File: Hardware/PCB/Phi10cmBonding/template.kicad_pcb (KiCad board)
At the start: 4 copper layers, 38.1 x 38.1 mm, 0 parts

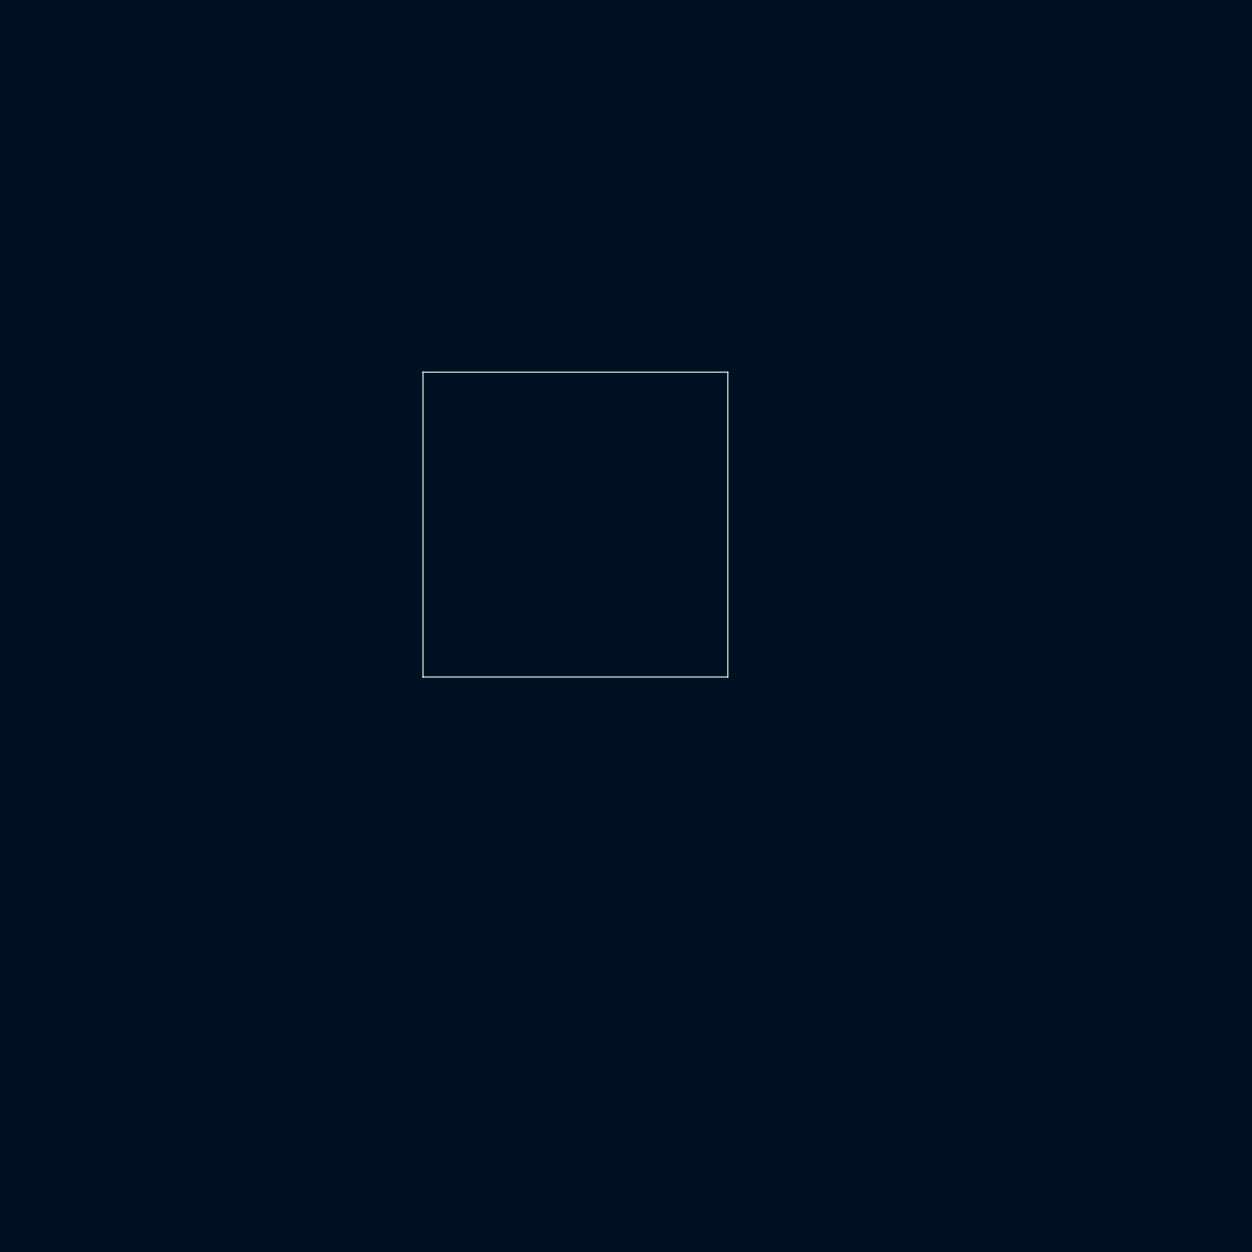
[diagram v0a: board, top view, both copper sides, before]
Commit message: Achieve reasonable array generation.
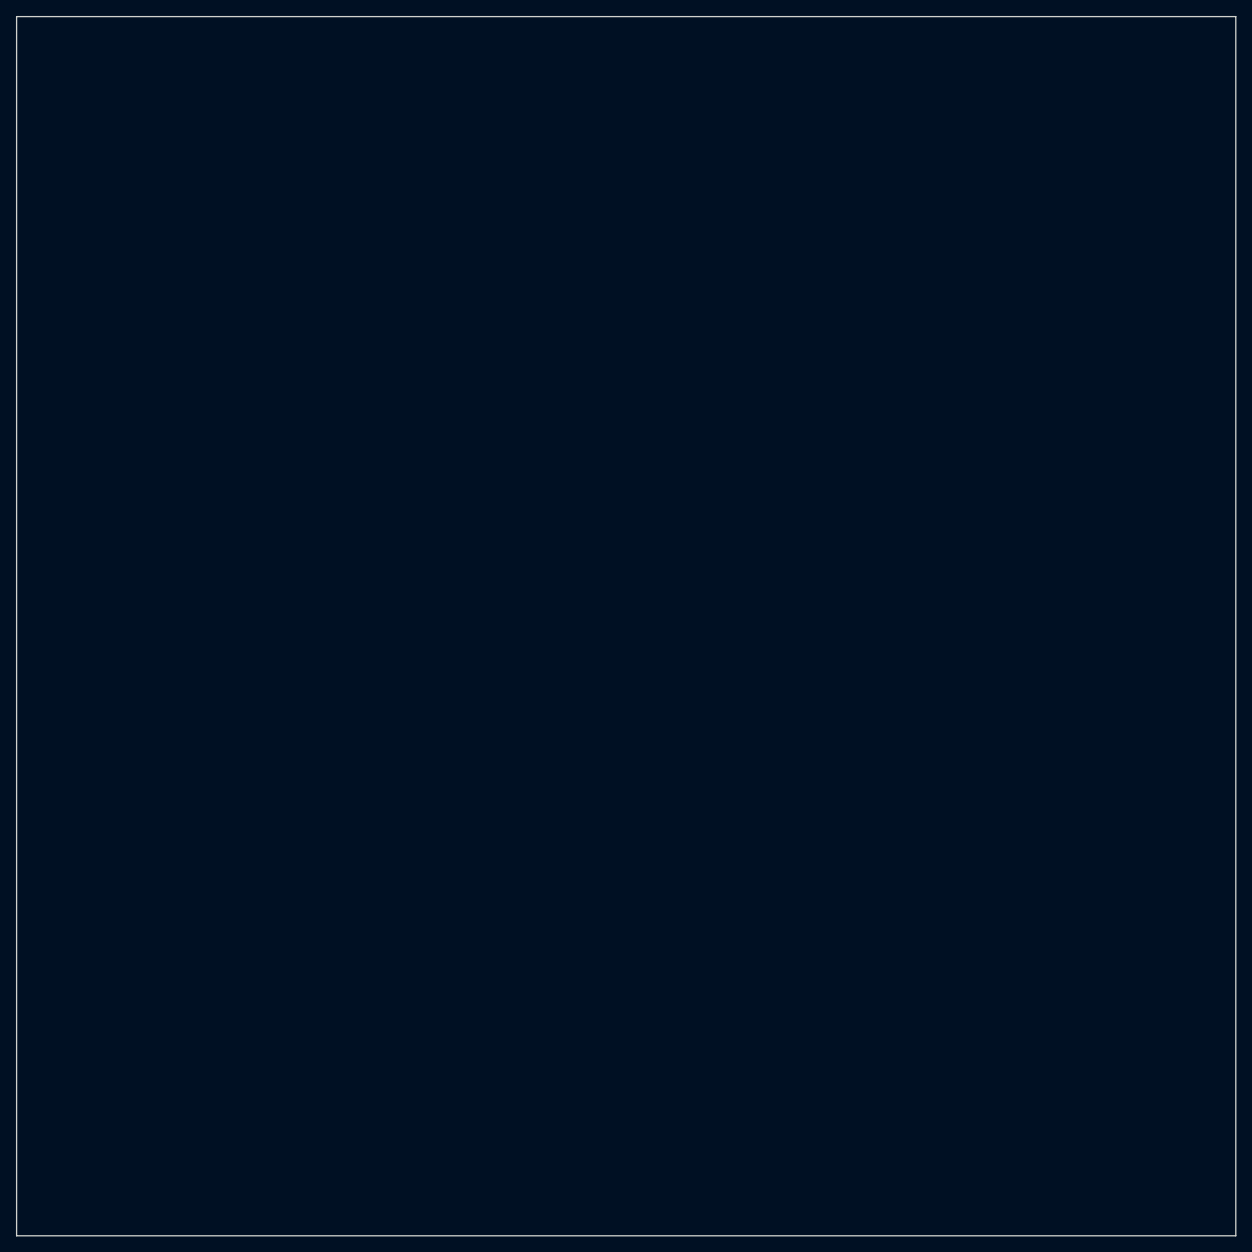
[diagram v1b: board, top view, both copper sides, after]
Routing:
- removed copper zone on In1.Cu, net /GND
- removed copper zone on In2.Cu, net /VDD
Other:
- board size 38.1 x 38.1 mm -> 152.4 x 152.4 mm
- copper layers 4 -> 20
- net class Default: trace_width 0.1524 -> 0.1016; via_dia 0.508 -> 0.5588; via_drill 0.381 -> 0.2032
- rule trace_min: 0.1524 -> 0.1016
- rule via_min_drill: 0.381 -> 0.2032
- rule via_min_size: 0.508 -> 0.5588
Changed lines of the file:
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@@
     (links 0)
     (no_connects 0)
-    (area 114.224999 76.124999 152.475001 114.375001)
-    (thickness 1.6)
+    (area 63.424999 31.674999 215.975001 184.225001)
+    (thickness 3.175)
     (drawings 4)
     (tracks 0)
     (zones 0)
     (modules 0)
-    (nets 3)
+    (nets 1)
   )
   (page USLetter)
@@
     (0 F.Cu signal)
     (1 In1.Cu power)
-    (2 In2.Cu jumper)
+    (2 In2.Cu signal)
+    (3 In3.Cu signal)
+    (4 In4.Cu signal)
+    (5 In5.Cu signal)
+    (6 In6.Cu signal)
+    (7 In7.Cu signal)
+    (8 In8.Cu signal)
+    (9 In9.Cu signal)
+    (10 In10.Cu signal)
+    (11 In11.Cu signal)
+    (12 In12.Cu signal)
+    (13 In13.Cu signal)
+    (14 In14.Cu signal)
+    (15 In15.Cu signal)
+    (16 In16.Cu signal)
+    (17 In17.Cu signal)
+    (18 In18.Cu signal)
     (31 B.Cu signal)
     (33 F.Adhes user)
@@
   )
   (setup
-    (last_trace_width 0.1524)
+    (last_trace_width 0.1016)
+    (user_trace_width 0.1016)
     (user_trace_width 0.1524)
     (user_trace_width 0.2032)
@@
     (zone_clearance 0.508)
     (zone_45_only no)
-    (trace_min 0.1524)
+    (trace_min 0.1016)
     (segment_width 0.2)
     (edge_width 0.15)
-    (via_size 0.508)
-    (via_drill 0.381)
-    (via_min_size 0.508)
-    (via_min_drill 0.381)
-    (user_via 0.508 0.381)
-    (user_via 0.762 0.508)
+    (via_size 0.5588)
+    (via_drill 0.2032)
+    (via_min_size 0.5588)
+    (via_min_drill 0.2032)
+    (user_via 0.5588 0.2032)
+    (user_via 0.7112 0.3556)
     (uvia_size 0.3048)
     (uvia_drill 0.1016)
@@
   )
   (net 0 "")
-  (net 1 /GND)
-  (net 2 /VDD)
   (net_class Default "This is the default net class."
     (clearance 0.1016)
-    (trace_width 0.1524)
-    (via_dia 0.508)
-    (via_drill 0.381)
+    (trace_width 0.1016)
+    (via_dia 0.5588)
+    (via_drill 0.2032)
     (uvia_dia 0.3048)
     (uvia_drill 0.1016)
+    (diff_pair_gap 0.2032)
+    (diff_pair_width 0.1016)
   )
-  (gr_line (start 152.4 76.2) (end 114.3 76.2) (layer Edge.Cuts) (width 0.15))
-  (gr_line (start 152.4 114.3) (end 152.4 76.2) (layer Edge.Cuts) (width 0.15))
-  (gr_line (start 114.3 114.3) (end 152.4 114.3) (layer Edge.Cuts) (width 0.15))
-  (gr_line (start 114.3 76.2) (end 114.3 114.3) (layer Edge.Cuts) (width 0.15))
-  (zone (net 1) (net_name /GND) (layer In1.Cu) (hatch edge 0.508)
-    (connect_pads (clearance 0.508))
-    (min_thickness 0.254)
-    (fill yes (arc_segments 16) (thermal_gap 0.508) (thermal_bridge_width 0.508))
-    (polygon
-      (pts
-        (xy 114.3 76.2) (xy 152.4 76.2) (xy 152.4 114.3) (xy 114.3 114.3)
-      )
-    )
-  )
-  (zone (net 2) (net_name /VDD) (layer In2.Cu) (hatch edge 0.508)
-    (connect_pads (clearance 0.508))
-    (min_thickness 0.254)
-    (fill yes (arc_segments 16) (thermal_gap 0.508) (thermal_bridge_width 0.508))
-    (polygon
-      (pts
-        (xy 114.3 76.2) (xy 152.4 76.2) (xy 152.4 114.3) (xy 114.3 114.3)
-      )
-    )
-  )
+  (gr_line (start 63.5 31.75) (end 215.9 31.75) (layer Edge.Cuts) (width 0.15))
+  (gr_line (start 215.9 31.75) (end 215.9 184.15) (layer Edge.Cuts) (width 0.15))
+  (gr_line (start 63.5 184.15) (end 215.9 184.15) (layer Edge.Cuts) (width 0.15))
+  (gr_line (start 63.5 31.75) (end 63.5 184.15) (layer Edge.Cuts) (width 0.15))
 )
